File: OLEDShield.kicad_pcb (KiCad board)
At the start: 2 copper layers, 68.6 x 53.3 mm, 192 parts, among them P1 CONN_5X2, P2 CONN_5X2, P3 CONN_1, P4 CONN_1, P5 CONN_1, SW1 SW_PUSHBUTTON

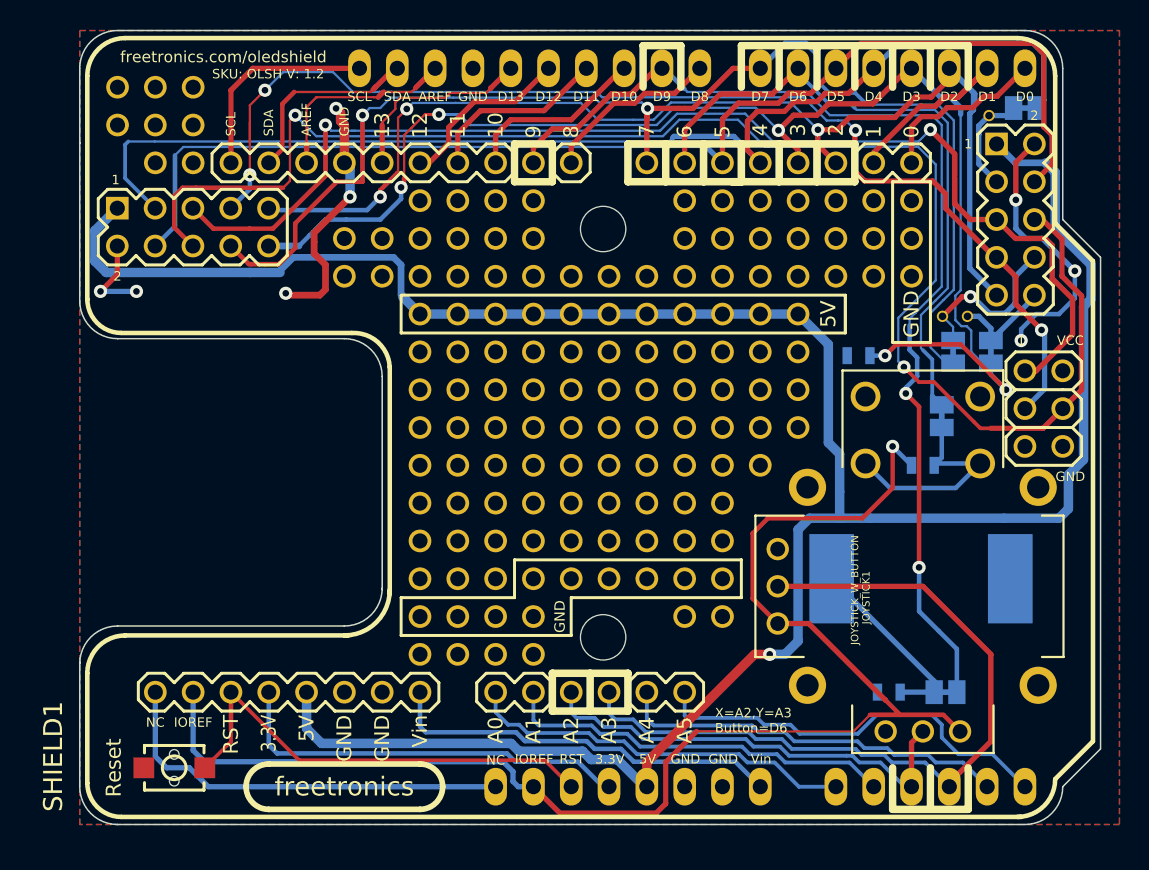
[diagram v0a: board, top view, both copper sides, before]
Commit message: Grow silkscreen labels where possible, bump version to 1.3
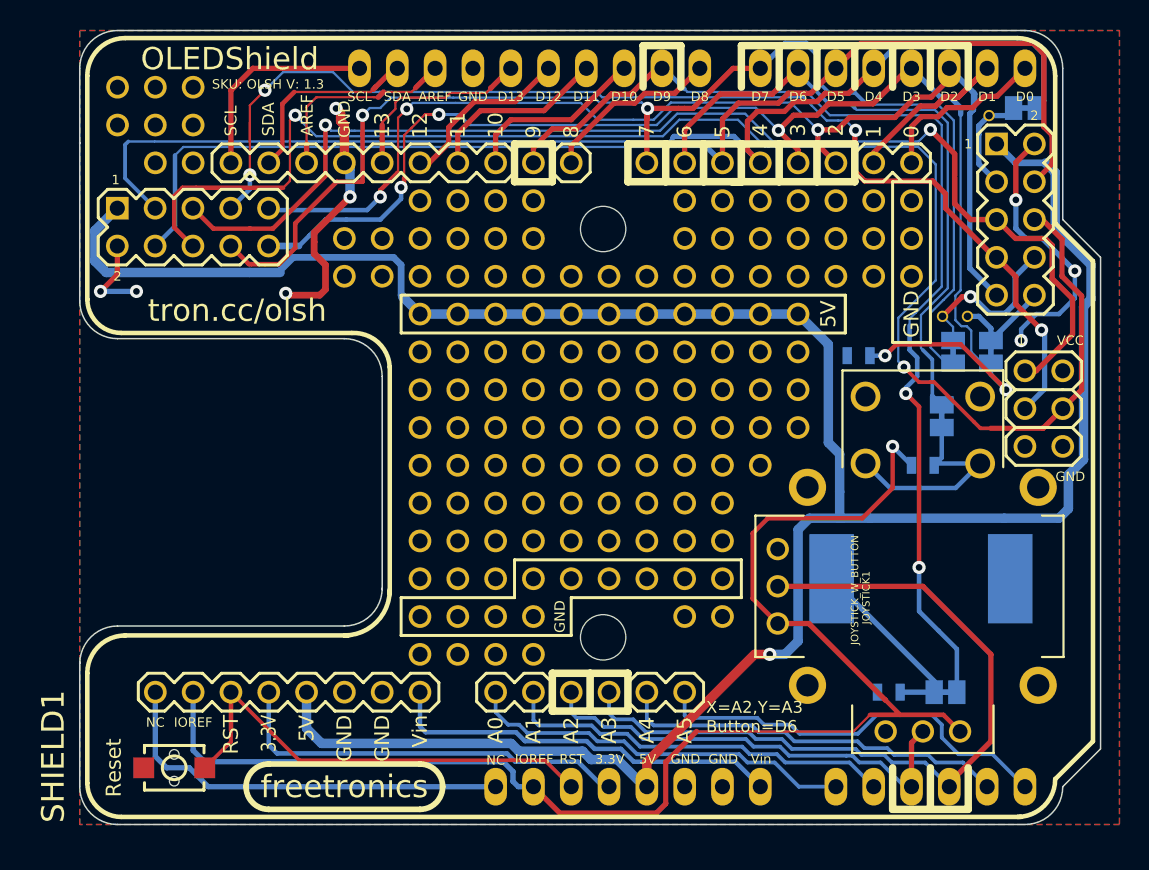
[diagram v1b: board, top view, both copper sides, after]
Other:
- board text added: "OLEDShield"
- board text added: "SKU: OLSH V: 1.3"
- board text added: "tron.cc/olsh"
- board text removed: "SKU: OLSH V: 1.2"
- board text removed: "freetronics.com/oledshield"
